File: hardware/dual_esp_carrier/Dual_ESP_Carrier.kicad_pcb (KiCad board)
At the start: 2 copper layers, 100 x 100 mm, 23 parts, among them J1 ESP32_T_LANDSCAPE, J2 ESP32_B_LANDSCAPE, J3 SX1278_LORA_2x4, J6 GPS_LC29H_7PIN, SW1 subir ancora, SW2 MODE, SW3 largar ancora, SW4 BOOT

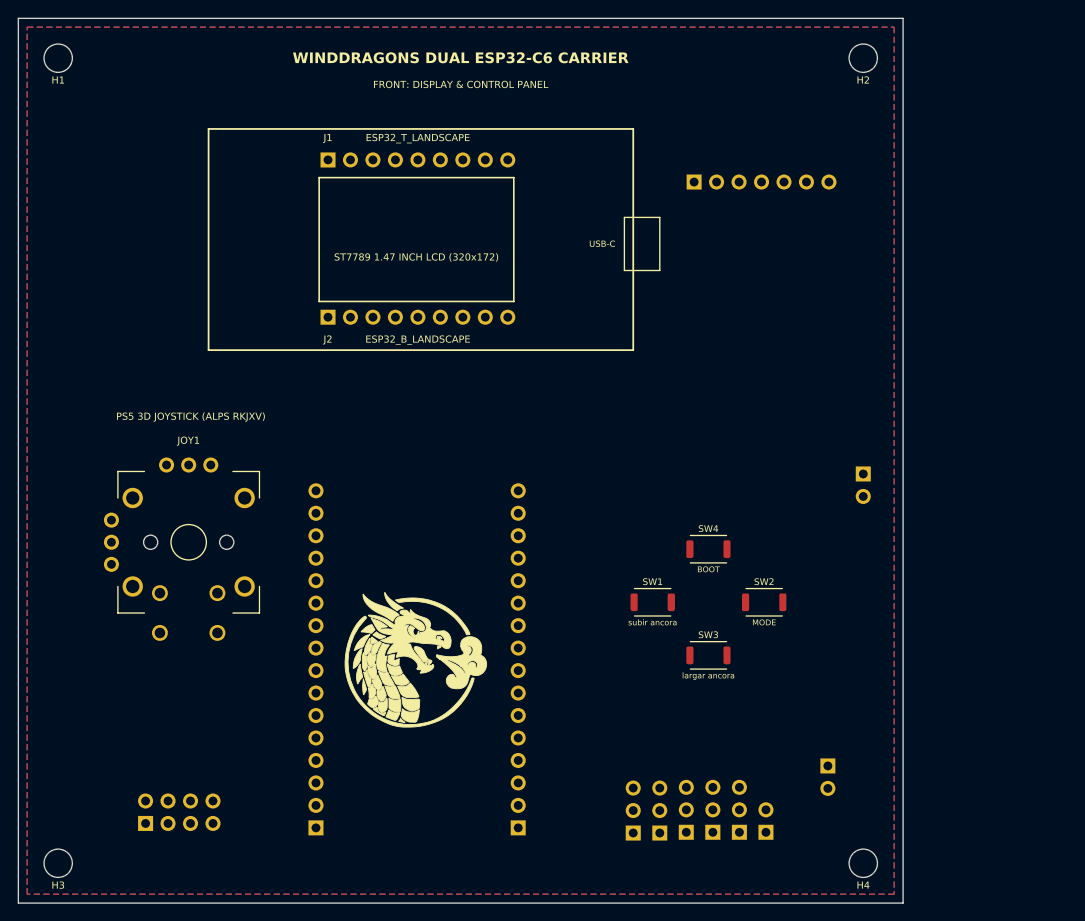
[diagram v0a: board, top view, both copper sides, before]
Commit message: feat: update hardware layout and gerber files for dual ESP carrier board
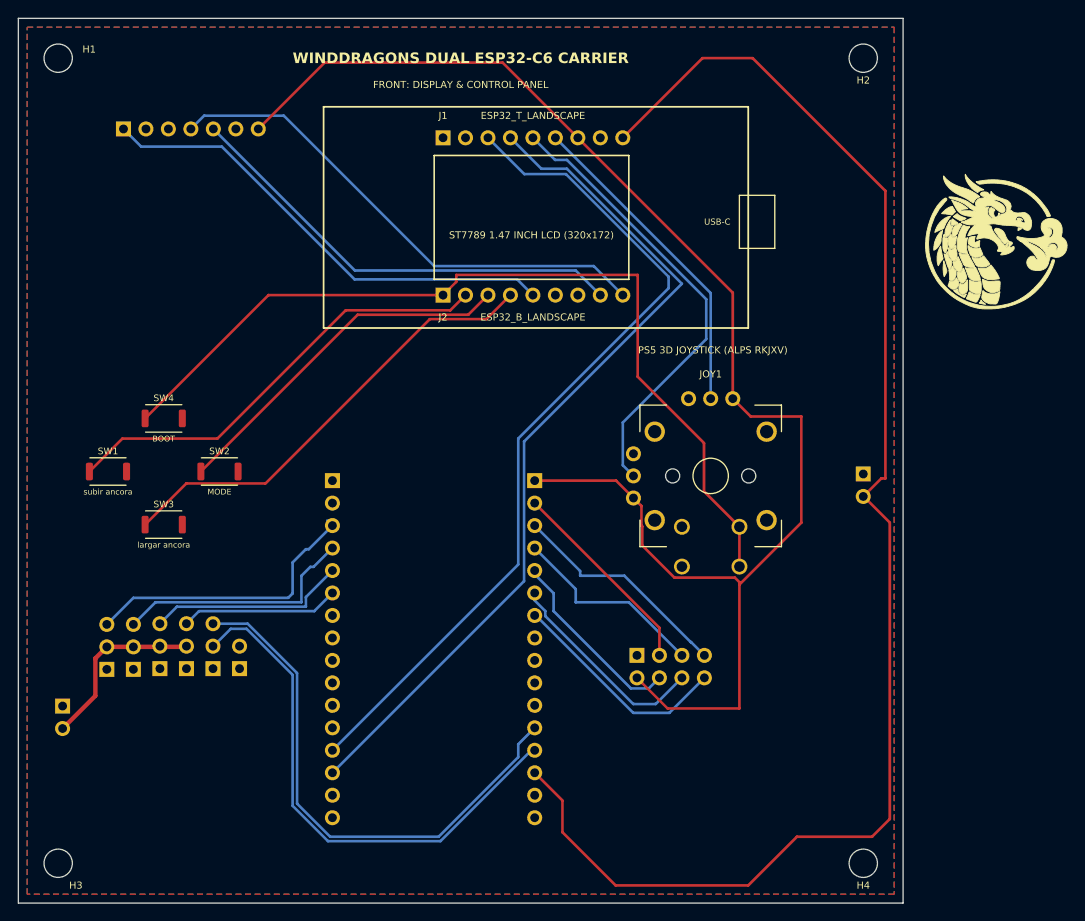
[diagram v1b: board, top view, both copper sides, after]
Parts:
- moved J_PWR_SRV 86.8 mm to (5.00, 77.7)
- moved J3 66.0 mm to (77.5, 72.0), turned to -90 degrees
- moved J6 64.8 mm to (11.9, 12.5)
- moved SW1 63.3 mm to (10.1, 51.2)
- moved SW3 63.3 mm to (16.4, 57.2)
- moved SW4 63.3 mm to (16.4, 45.2)
- moved SW2 63.3 mm to (22.7, 51.2)
- moved ESC 62.3 mm to (10.0, 73.6)
- moved J_BATT 62.3 mm to (22.0, 73.5)
- moved J_WATER 62.3 mm to (25.0, 73.5)
- moved RCK 62.3 mm to (19.0, 73.5)
- moved RUD 62.3 mm to (13.0, 73.6)
- moved WIN 62.3 mm to (16.0, 73.5)
- moved JOY1 59.5 mm to (78.3, 51.7)
- moved J_DK_L 46.4 mm to (58.4, 52.2), turned to 0 degrees
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- renumbered J_DK_R to J_DK_L, J_DK_L to J_DK_R
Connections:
- J_BATT pad 1: /BATT_VOLT -> /GND
- J_BATT pad 3: /GND -> /BATT_VOLT
- J_DK_L pad 1: /GND -> /+3V3
- J_DK_L pad 10: (no net) -> /WATER_SENS
- J_DK_L pad 12: /GND -> /BATT_VOLT
- J_DK_L pad 13: (no net) -> /BATT_CURR
- J_DK_L pad 14: (no net) -> /+5V
- J_DK_L pad 2: /LORA_NSS -> /LORA_RST
- J_DK_L pad 3: /LORA_SCK -> /LORA_MISO
- J_DK_L pad 4: /LORA_MOSI -> /LORA_SCK
- J_DK_L pad 5: /LORA_MISO -> /LORA_NSS
- J_DK_L pad 6: /LORA_RST -> /LORA_MOSI
- J_DK_R pad 1: /+3V3 -> /GND
- J_DK_R pad 10: /WATER_SENS -> (no net)
- J_DK_R pad 12: /INTER_TX_M2S -> /GND
- J_DK_R pad 13: /INTER_RX_S2M -> /INTER_TX_M2S
- J_DK_R pad 14: /+5V -> /INTER_RX_S2M
- J_DK_R pad 7: /BATT_VOLT -> (no net)
- J_DK_R pad 8: /BATT_CURR -> (no net)
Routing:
- net /+3V3: track 0.00 -> 167.7 mm
- net /+5V: track 0.00 -> 163.8 mm
- net /IO9_BOOT: track 0.00 -> 100.6 mm
- net /INTER_RX_S2M: track 0.00 -> 97.8 mm
- net /INTER_TX_M2S: track 0.00 -> 96.2 mm
- net /BATT_VOLT: track 0.00 -> 60.9 mm
- net /BATT_CURR: track 0.00 -> 60.0 mm
- net /GPS_TX: track 0.00 -> 57.8 mm
- net /GPS_PPS: track 0.00 -> 54.1 mm
- net /IO20_DN: track 0.00 -> 52.0 mm
- net /GPS_RX: track 0.00 -> 51.5 mm
- net /JOY_Y: track 0.00 -> 51.5 mm
- net /IO18_UP: track 0.00 -> 50.8 mm
- net /IO19_MODE: track 0.00 -> 40.7 mm
- net /JOY_X: track 0.00 -> 36.8 mm
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
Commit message: feat: update dual ESP carrier PCB layout and add power and UART test sources
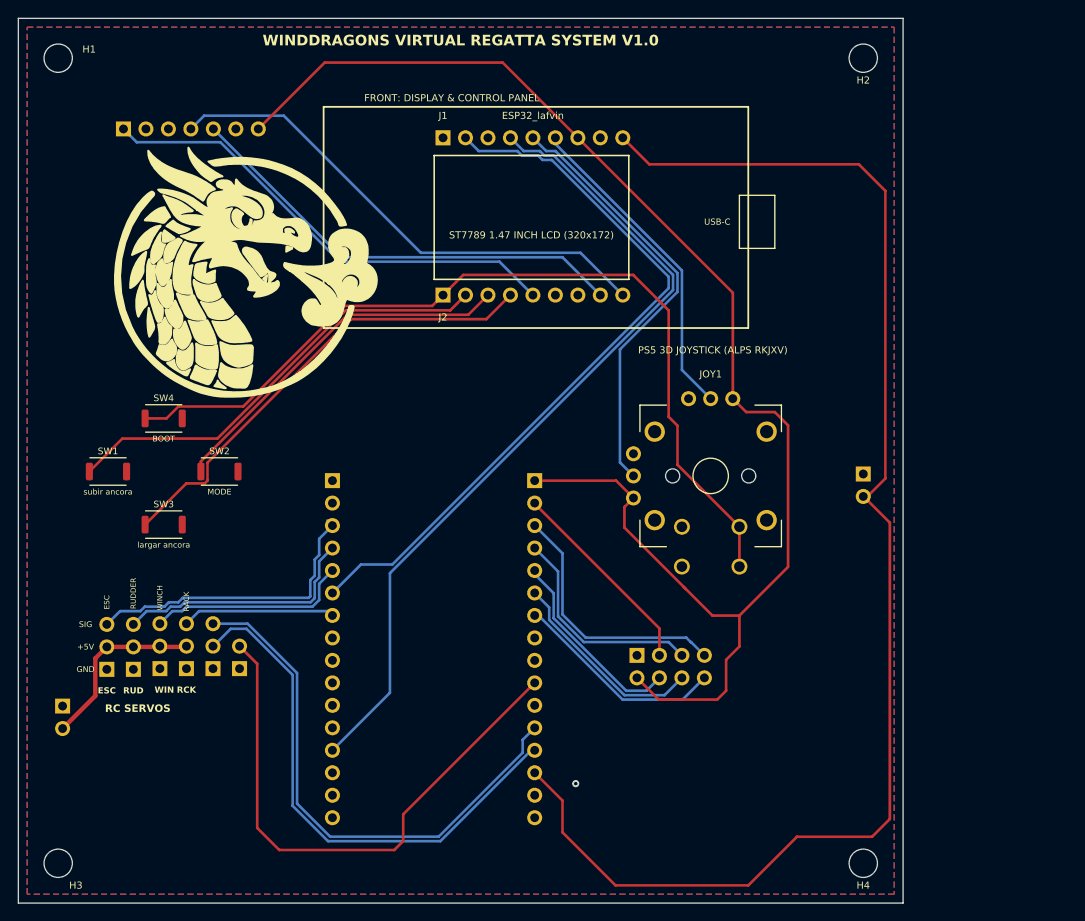
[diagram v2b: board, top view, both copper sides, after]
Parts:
- ESC: value ESC (IO4) -> ESC; moved to F.Cu
- J1: value ESP32_T_LANDSCAPE -> ESP32_lafvin
- RCK: value RACK (IO7) -> RACK; moved to F.Cu
- RUD: value RUDDER (IO5) -> RUDDER; moved to F.Cu
- WIN: value WINCH (IO6) -> WINCH; moved to F.Cu
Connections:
- J1 pad 2: /IO4_FREE -> /INTER_TX_M2S
- J1 pad 3: /INTER_TX_M2S -> /IO3_FREE
- J_DK_R pad 13: /INTER_TX_M2S -> /INTER_RX_S2M
- J_DK_R pad 14: /INTER_RX_S2M -> (no net)
- J_DK_R pad 6: /SERVO_RACK -> /INTER_TX_M2S
- J_DK_R pad 7: (no net) -> /SERVO_RACK
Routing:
- net /WATER_SENS: track 0.00 -> 63.4 mm
- net /INTER_TX_M2S: track 96.2 -> 83.0 mm
- net /+5V: track 163.8 -> 156.4 mm
- net /LORA_MISO: track 25.6 -> 29.3 mm
- net /INTER_RX_S2M: track 97.8 -> 94.5 mm
- net /+3V3: track 167.7 -> 164.6 mm
- net /JOY_Y: track 51.5 -> 48.9 mm
- net /LORA_SCK: track 22.5 -> 24.6 mm
- net /LORA_DIO0: track 25.4 -> 24.1 mm
- net /IO20_DN: track 52.0 -> 53.2 mm
- net /SERVO_ESC: track 33.0 -> 34.2 mm
- net /LORA_MOSI: track 23.9 -> 23.1 mm
- net /IO9_BOOT: track 100.6 -> 99.8 mm
- net /LORA_NSS: track 21.6 -> 22.2 mm
- net /IO19_MODE: track 40.7 -> 41.4 mm
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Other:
- board text added: "+5V"
- board text added: "GND"
- board text added: "RC SERVOS"
- board text added: "SIG"
- board text added: "WINDDRAGONS VIRTUAL REGATTA SYSTEM V1.0"
- board text removed: "WINDDRAGONS DUAL ESP32-C6 CARRIER"

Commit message: feat: enhance battery monitoring web UI with dynamic cell configurations and capacity controls
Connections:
- J1 pad 2: /INTER_TX_M2S -> /IO4_FREE
- J1 pad 3: /IO3_FREE -> /JOY_X
- J1 pad 4: /INTER_RX_S2M -> /INTER_TX_M2S
- J1 pad 5: /JOY_Y -> /INTER_RX_S2M
- J1 pad 6: /JOY_X -> /JOY_Y
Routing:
- net /JOY_X: track 36.8 -> 53.7 mm
- net /INTER_RX_S2M: track 94.5 -> 99.6 mm
- net /JOY_Y: track 48.9 -> 53.6 mm
- net /INTER_TX_M2S: track 83.0 -> 85.6 mm
- net /GND: vias 1 -> 0

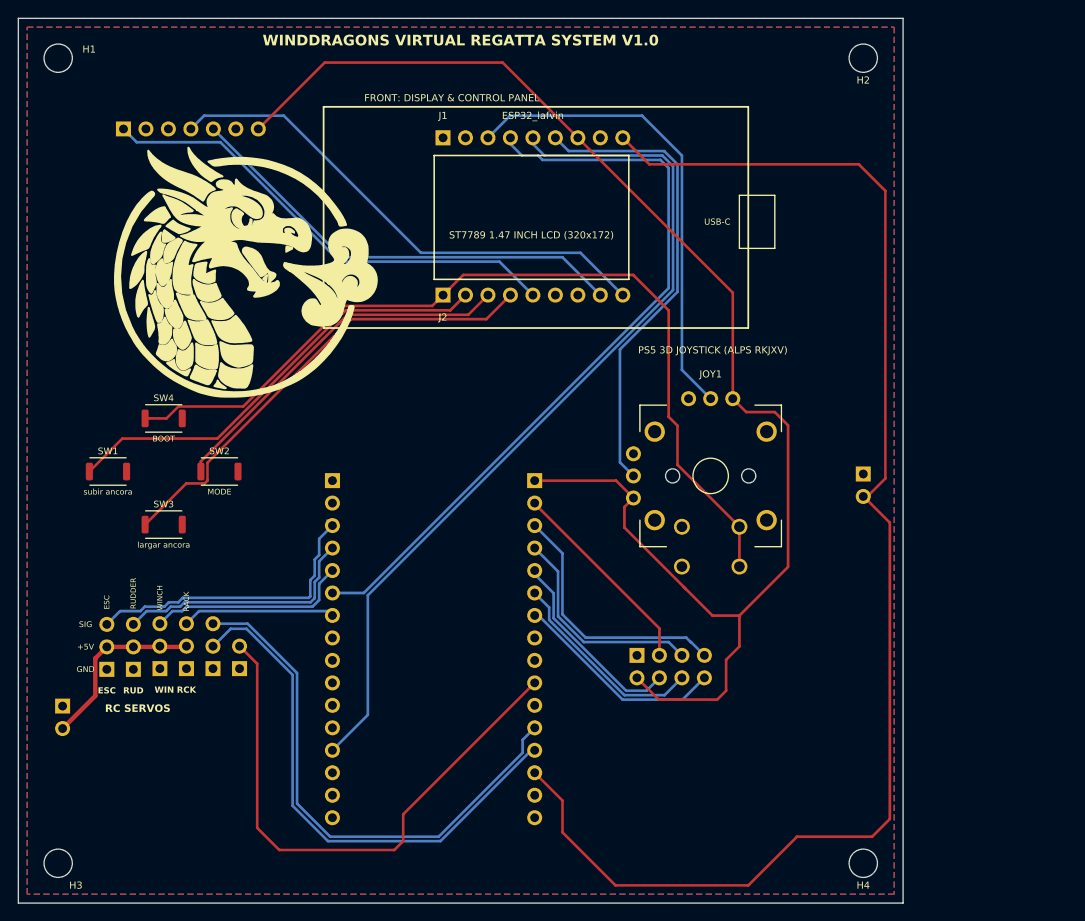
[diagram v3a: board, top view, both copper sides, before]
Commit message: feat: add limit switch and strobe LED support to hardware and firmware
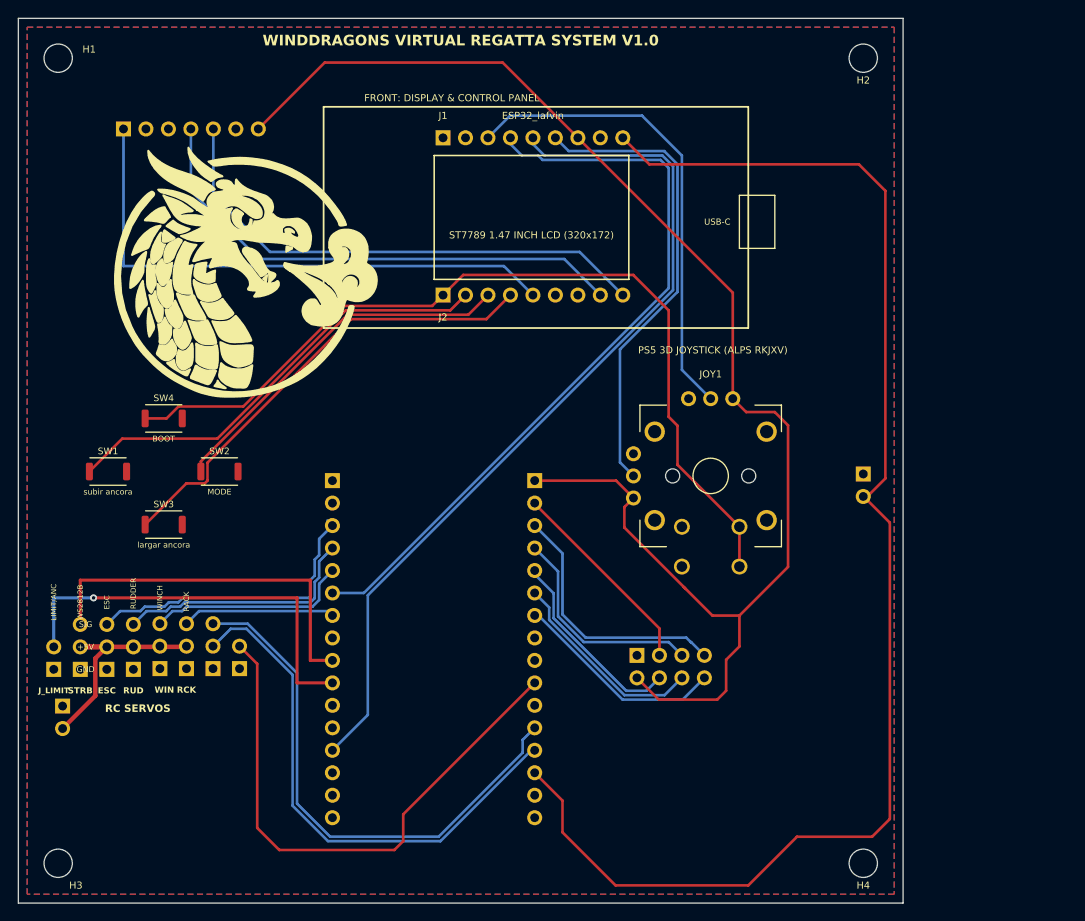
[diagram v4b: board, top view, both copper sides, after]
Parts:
- added J_LIMIT: LIMIT/ANC, Connector_PinHeader_2.54mm:PinHeader_1x02_P2.54mm_Vertical, F.Cu at (4.00, 73.6)
- added STRB: WS2812B, Connector_PinHeader_2.54mm:PinHeader_1x03_P2.54mm_Vertical, F.Cu at (7.00, 73.6)
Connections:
- J6 pad 4: /GPS_TX -> /GPS_RX
- J6 pad 5: /GPS_RX -> /GPS_TX
- J_DK_R pad 10: (no net) -> /ANCHOR_LIMIT
- J_DK_R pad 9: (no net) -> /STROBE_DIN
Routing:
- net /ANCHOR_LIMIT: track 0.00 -> 46.7 mm, vias 0 -> 1
- net /STROBE_DIN: track 0.00 -> 42.6 mm
- net /GPS_PPS: track 54.1 -> 63.1 mm
- net /GPS_RX: track 51.5 -> 58.2 mm
- net /+5V_SERVO: track 20.3 -> 23.3 mm
- net /GPS_TX: track 57.8 -> 58.5 mm

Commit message: feat: separate 3.3V power domains for Lafvin and DevKitC C6 on carrier board
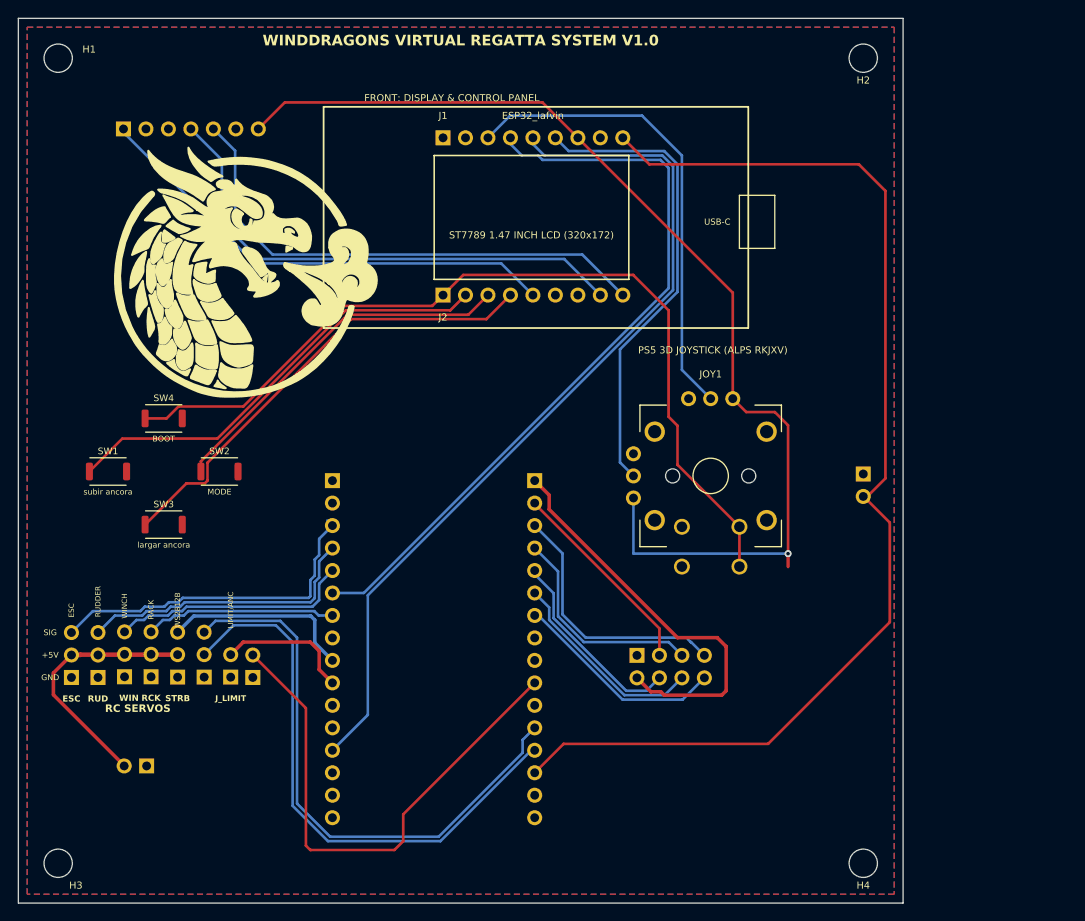
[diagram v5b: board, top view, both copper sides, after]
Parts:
- moved J_LIMIT 20.0 mm to (24.0, 74.5)
- moved J_PWR_SRV 11.7 mm to (14.5, 84.5), turned to -90 degrees
- moved STRB 11.0 mm to (18.0, 74.5)
- moved ESC 4.10 mm to (6.00, 74.5)
- moved RCK 4.10 mm to (15.0, 74.4)
- moved RUD 4.10 mm to (9.00, 74.5)
- moved WIN 4.10 mm to (12.0, 74.4)
- moved J_WATER 1.80 mm to (26.5, 74.5)
- moved J_BATT 1.39 mm to (21.0, 74.5)
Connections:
- J3 pad 2: /+3V3 -> /+3V3_C6
- J_DK_L pad 1: /+3V3 -> /+3V3_C6
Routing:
- net /+3V3_C6: track 0.00 -> 46.4 mm
- net /+3V3: track 164.6 -> 124.5 mm, vias 0 -> 1
- net /ANCHOR_LIMIT: track 46.7 -> 15.2 mm, vias 1 -> 0
- net /+5V: track 156.4 -> 130.7 mm
- net /STROBE_DIN: track 42.6 -> 21.8 mm
- net /GPS_PPS: track 63.1 -> 54.3 mm
- net /+5V_SERVO: track 23.3 -> 28.9 mm
- net /SERVO_RACK: track 17.3 -> 22.4 mm
- net /SERVO_RUDDER: track 28.2 -> 32.6 mm
- net /SERVO_WINCH: track 23.1 -> 27.4 mm
- net /SERVO_ESC: track 34.2 -> 38.5 mm
- net /BATT_VOLT: track 60.9 -> 64.9 mm
- net /BATT_CURR: track 60.0 -> 63.9 mm
- net /WATER_SENS: track 63.4 -> 59.7 mm

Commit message: feat: update Dual ESP carrier PCB layout, gerbers, and pinout documentation
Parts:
- J_BATT, J_WATER: moved to F.Cu
- moved J_LIMIT 2.76 mm to (21.2, 74.5)
- moved J_WATER 2.72 mm to (23.8, 74.5)
- moved J_BATT 2.30 mm to (18.7, 74.5)
- moved STRB 1.84 mm to (16.2, 74.5)
- moved RCK 1.38 mm to (13.6, 74.5)
- moved WIN 0.92 mm to (11.1, 74.5)
- moved RUD 0.46 mm to (8.54, 74.5)
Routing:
- net /+3V3: track 124.5 -> 91.6 mm, vias 1 -> 0
- net /ANCHOR_LIMIT: track 15.2 -> 18.0 mm
- net /WATER_SENS: track 59.7 -> 62.4 mm
- net /BATT_VOLT: track 64.9 -> 67.2 mm
- net /BATT_CURR: track 63.9 -> 66.2 mm
- net /+5V_SERVO: track 28.9 -> 26.9 mm
- net /STROBE_DIN: track 21.8 -> 23.7 mm
- net /SERVO_RACK: track 22.4 -> 23.8 mm
- net /GPS_RX: track 58.2 -> 59.4 mm
- net /SERVO_WINCH: track 27.4 -> 28.4 mm
- net /GPS_TX: track 58.5 -> 59.4 mm
